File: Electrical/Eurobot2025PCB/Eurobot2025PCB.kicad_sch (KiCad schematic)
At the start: 24 parts, among them J1 Screw_Terminal_01x02, J2 Conn_01x04_Socket, J3 Conn_01x04_Socket, J4 Conn_01x04_Socket, J5 Screw_Terminal_01x02, M1 Motor_Servo, M2 Motor_Servo, M3 Motor_Servo, SW1 SW_SPDT, SW2 SW_SPDT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

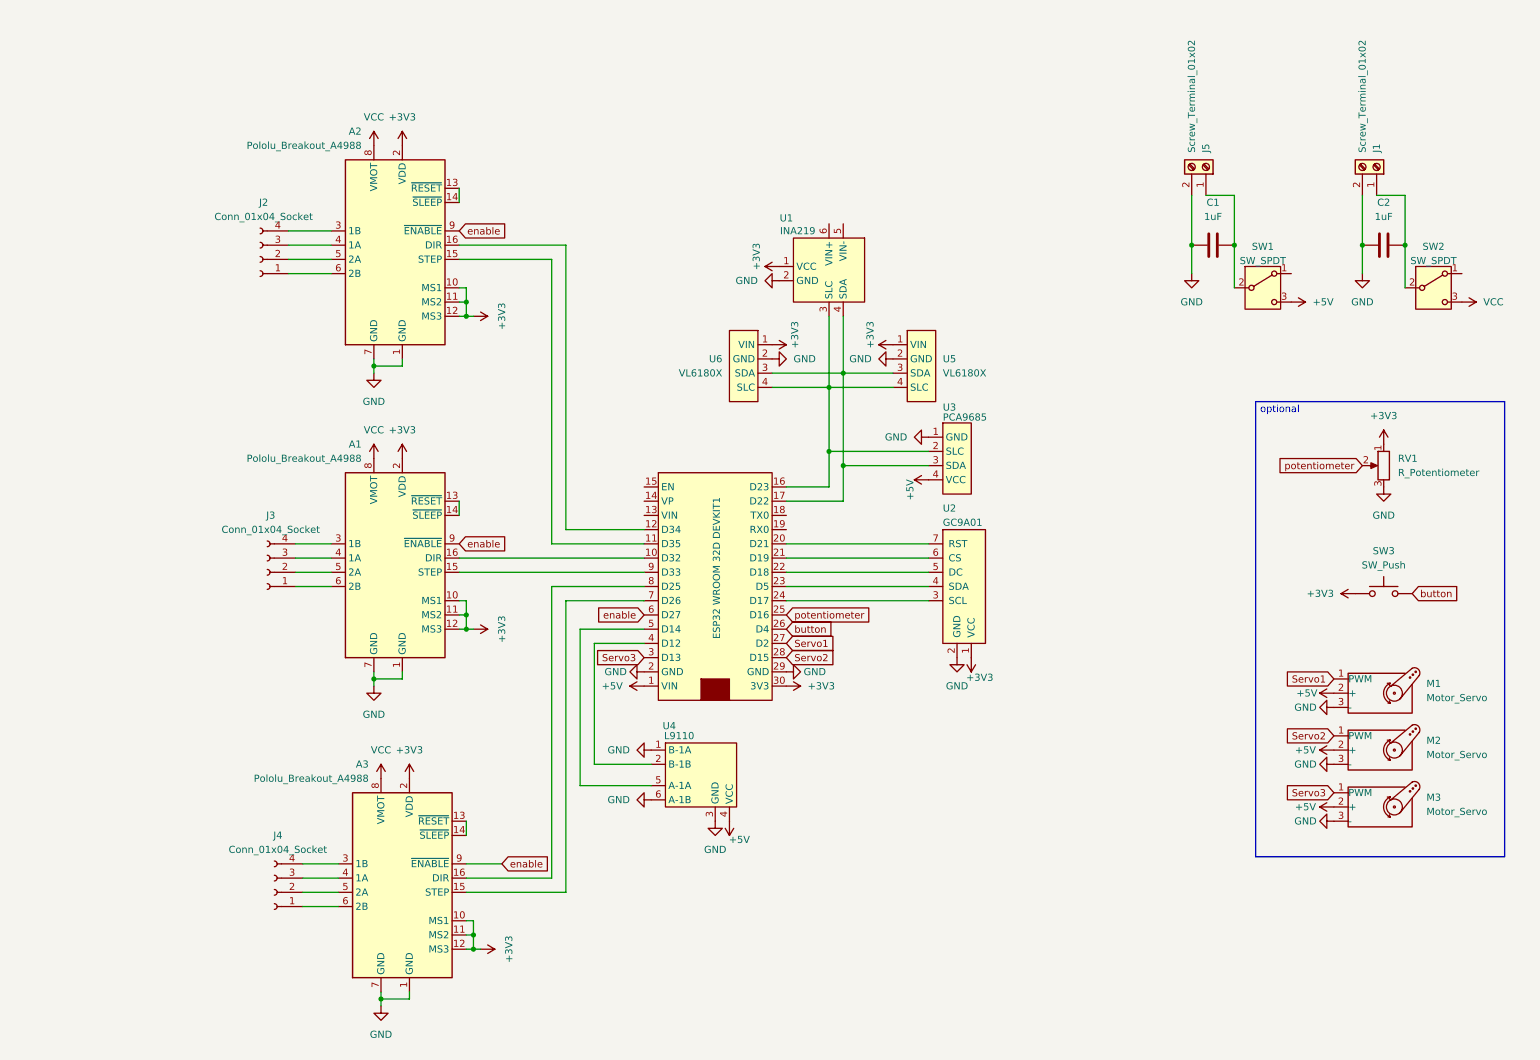
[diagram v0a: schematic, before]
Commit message: Add 4th step motor and 12V to 5V converter to PCB
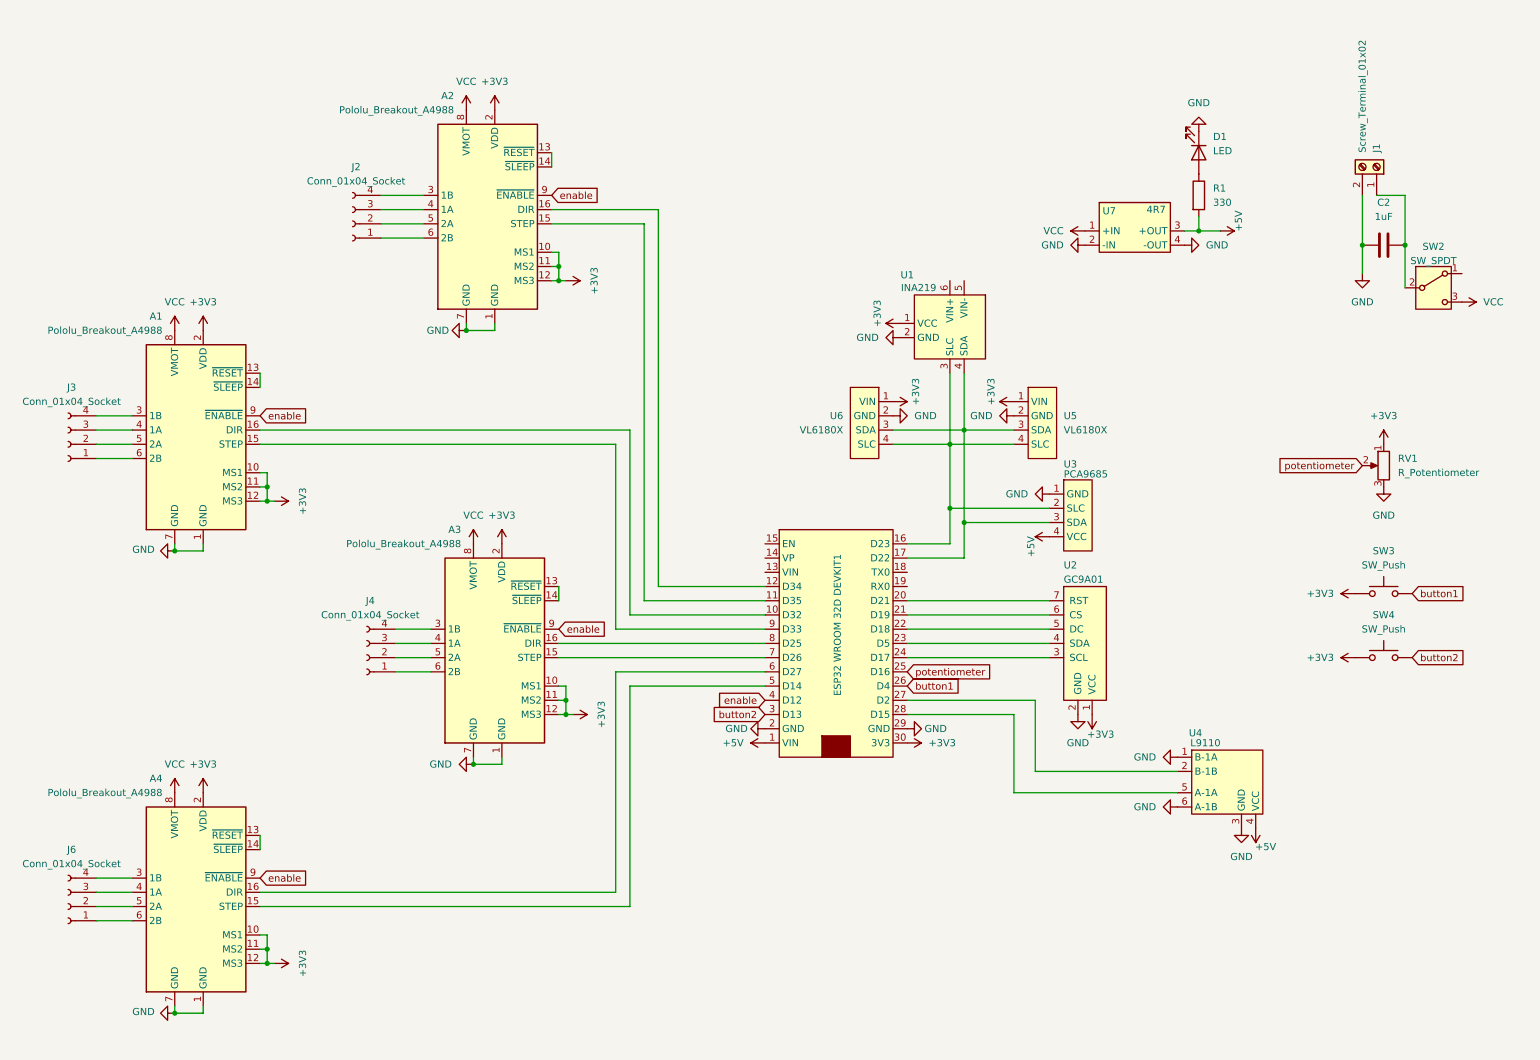
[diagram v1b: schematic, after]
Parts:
- removed C1: 1uF, Capacitor_THT:C_Radial_D5.0mm_H11.0mm_P2.00mm, symbol Device:C
- removed J5: Screw_Terminal_01x02, TerminalBlock_MetzConnect:TerminalBlock_MetzConnect_Type059_RT06302HBWC_1x02_P3.50mm_Horizontal, symbol Connector:Screw_Terminal_01x02
- removed M1, M2, M3: Motor_Servo, Connector_PinHeader_2.54mm:PinHeader_1x03_P2.54mm_Vertical, symbol Motor:Motor_Servo
- removed SW1: SW_SPDT, Button_Switch_THT:SW_XKB_DM1-16UP-1, symbol Switch:SW_SPDT
- added A4: Pololu_Breakout_A4988, ECN:A4988, symbol Driver_Motor:Pololu_Breakout_A4988
- added D1: LED, LED_THT:LED_D1.8mm_W1.8mm_H2.4mm_Horizontal_O6.35mm_Z8.2mm, symbol Device:LED
- added J6: Conn_01x04_Socket, Connector_JST:JST_XH_B4B-XH-A_1x04_P2.50mm_Vertical, symbol Connector:Conn_01x04_Socket
- added R1: 330, Resistor_THT:R_Axial_DIN0207_L6.3mm_D2.5mm_P10.16mm_Horizontal, symbol Device:R
- added SW4: SW_Push, Button_Switch_THT:SW_PUSH_6mm, symbol Switch:SW_Push
- added U7: 4R7, ECN:4R7, symbol ECN:4R7
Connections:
- net Servo1 is gone; now on an unnamed net: ESP32 WROOM 32D DEVKIT1.27 (D2)
- net +3V3: now also A4.10 (MS1), A4.11 (MS2), A4.12 (MS3), A4.2 (VDD), SW4.1
- net +5V: now also R1.2, U7.3 (+OUT)
- net GND: now also A4.1 (GND), A4.7 (GND), D1.1 (K), U7.2 (-IN), U7.4 (-OUT)
- net VCC: now also A4.8 (VMOT), U7.1 (+IN)
- net enable: now also ESP32 WROOM 32D DEVKIT1.4 (D12), A4.9 (~{ENABLE}); no longer ESP32 WROOM 32D DEVKIT1.6 (D27)
- net at U4.2 (B-1B): no longer ESP32 WROOM 32D DEVKIT1.4 (D12)
- net at ESP32 WROOM 32D DEVKIT1.5 (D14): now also A4.15 (STEP); no longer U4.5 (A-1A)
- net Servo2: no longer names the net of ESP32 WROOM 32D DEVKIT1.28 (D15)
- net Servo2: now also U4.5 (A-1A)
- net Servo3 renamed button2
- net button2: now also SW4.2
- net button renamed button1
- new net: A4.6 (2B), J6.1 (Pin_1)
- new net: A4.5 (2A), J6.2 (Pin_2)
- new net: A4.4 (1A), J6.3 (Pin_3)
- new net: A4.3 (1B), J6.4 (Pin_4)
- new net: A4.13 (~{RESET}), A4.14 (~{SLEEP})
- new net: A4.16 (DIR), ESP32 WROOM 32D DEVKIT1.6 (D27)
- new net: D1.2 (A), R1.1
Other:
- note removed: "optional"
- moved on the sheet: A1, A2, A3, ESP32 WROOM 32D DEVKIT1, J2, J3, J4, U1, U2, U3, U4, U5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

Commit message: updated pcb
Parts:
- added J5: Conn_01x02_Socket, Connector_PinHeader_2.54mm:PinHeader_1x02_P2.54mm_Vertical, symbol Connector:Conn_01x02_Socket
- D1: footprint LED_THT:LED_D1.8mm_W1.8mm_H2.4mm_Horizontal_O6.35mm_Z8.2mm -> LED_THT:LED_D5.0mm
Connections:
- net at ESP32 WROOM 32D DEVKIT1.18 (TX0): now also J5.1 (Pin_1)
- net at ESP32 WROOM 32D DEVKIT1.19 (RX0): now also J5.2 (Pin_2)
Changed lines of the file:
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@@
+	)
+	(symbol
+		(lib_id "Connector:Conn_01x02_Socket")
+		(at 180.34 111.76 0)
+		(unit 1)
+		(exclude_from_sim no)
+		(in_bom yes)
+		(on_board yes)
+		(dnp no)
+		(fields_autoplaced yes)
+		(property "Reference" "J5"
+			(at 181.61 111.7599 0)
+			(effects
+				(font
+					(size 1.27 1.27)
+				)
+				(justify left)
+			)
+		)
+		(property "Value" "Conn_01x02_Socket"
+			(at 181.61 114.2999 0)
+			(effects
+				(font
+					(size 1.27 1.27)
+				)
+				(justify left)
+			)
+		)
+		(property "Footprint" "Connector_PinHeader_2.54mm:PinHeader_1x02_P2.54mm_Vertical"
+			(at 180.34 111.76 0)
+			(effects
+				(font
+					(size 1.27 1.27)
+				)
+				(hide yes)
+			)
+		)
+		(property "Datasheet" "~"
+			(at 180.34 111.76 0)
+			(effects
+				(font
+					(size 1.27 1.27)
+				)
+				(hide yes)
+			)
+		)
+		(property "Description" "Generic connector, single row, 01x02, script generated"
+			(at 180.34 111.76 0)
+			(effects
+				(font
+					(size 1.27 1.27)
+				)
+				(hide yes)
+			)
+		)
+		(pin "1"
+		)
+		(pin "2"
+		)
+		(instances
+			(project ""
+				(path "/0e44cb1f-d50f-4cbf-b876-98930a2e4cdb"
+					(reference "J5")
+					(unit 1)
+				)
+			)
+		)
 	)
 	(symbol
@@
 			)
 		)
-		(property "Footprint" "LED_THT:LED_D1.8mm_W1.8mm_H2.4mm_Horizontal_O6.35mm_Z8.2mm"
+		(property "Footprint" "LED_THT:LED_D5.0mm"
 			(at 227.33 36.83 0)
 			(effects

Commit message: update pcb :alien:
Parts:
- removed A2: Pololu_Breakout_A4988, ECN:A4988, symbol Driver_Motor:Pololu_Breakout_A4988
- removed J2: Conn_01x04_Socket, Connector_JST:JST_XH_B4B-XH-A_1x04_P2.50mm_Vertical, symbol Connector:Conn_01x04_Socket
- added D2: 1N5817, Diode_THT:D_DO-41_SOD81_P10.16mm_Horizontal, symbol Diode:1N5817
- added J2: Conn_01x04, symbol Connector_Generic:Conn_01x04
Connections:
- net at ESP32 WROOM 32D DEVKIT1.11 (D35): now also J2.3 (Pin_3)
- net at ESP32 WROOM 32D DEVKIT1.12 (D34): now also J2.4 (Pin_4)
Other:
- moved on the sheet: D1, R1, U7

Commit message: updated PCB
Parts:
- removed J2: Conn_01x04, symbol Connector_Generic:Conn_01x04
- added H1, H2, H3, H4: MountingHole, MountingHole:MountingHole_3.2mm_M3, symbol Mechanical:MountingHole
- added SW1: SW_Push_Dual, Connector_PinHeader_2.54mm:PinHeader_2x02_P2.54mm_Vertical, symbol Switch:SW_Push_Dual
- added SW5: SW_Push, Connector_JST:JST_XH_B2B-XH-A_1x02_P2.50mm_Vertical, symbol Switch:SW_Push
- added U8: PCF8574, Connector_PinHeader_2.54mm:PinHeader_1x04_P2.54mm_Vertical, symbol ECN:PCF8574
- U3: footprint Connector_PinHeader_2.54mm:PinHeader_1x04_P2.54mm_Vertical -> Connector_PinHeader_2.54mm:PinHeader_1x05_P2.54mm_Vertical
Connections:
- net +3V3: now also U3.5 (3V3), SW1.1, SW1.3, U8.1 (Vcc); no longer A1.10 (MS1), A1.11 (MS2), A1.12 (MS3), A3.10 (MS1), A3.11 (MS2), A3.12 (MS3), A4.10 (MS1), A4.11 (MS2), A4.12 (MS3)
- net +5V: now also D2.2 (A); no longer ESP32 WROOM 32D DEVKIT1.1 (VIN)
- net GND: now also A1.10 (MS1), A1.11 (MS2), A1.12 (MS3), A3.10 (MS1), A3.11 (MS2), A3.12 (MS3), A4.10 (MS1), A4.11 (MS2), A4.12 (MS3), U8.2 (GND)
- net VCC: now also SW5.2; no longer SW2.3 (C)
- net at ESP32 WROOM 32D DEVKIT1.16 (D23), U1.3 (SLC), U3.2 (SLC)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: now also U8.4 (SCL)
- net at ESP32 WROOM 32D DEVKIT1.17 (D22), U1.4 (SDA), U3.3 (SDA)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: now also U8.3 (SDA)
- net LimitSwitch2: now reaches ESP32 WROOM 32D DEVKIT1.11 (D35)
- net LimitSwitch2: now also SW1.4
- net LimitSwitch1: now reaches ESP32 WROOM 32D DEVKIT1.12 (D34)
- net LimitSwitch1: now also SW1.2
- net at D2.1 (K): now also ESP32 WROOM 32D DEVKIT1.1 (VIN)
- new net: SW2.3 (C), SW5.1
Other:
- moved on the sheet: C2, D1, D2, J1, R1, RV1, SW2, SW3, SW4, U1, U5, U6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
